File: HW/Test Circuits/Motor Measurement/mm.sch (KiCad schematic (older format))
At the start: 20 parts, among them J1 IN, J2 MOTOR, J3 PWR, J4 OUT, U1 MCP6002

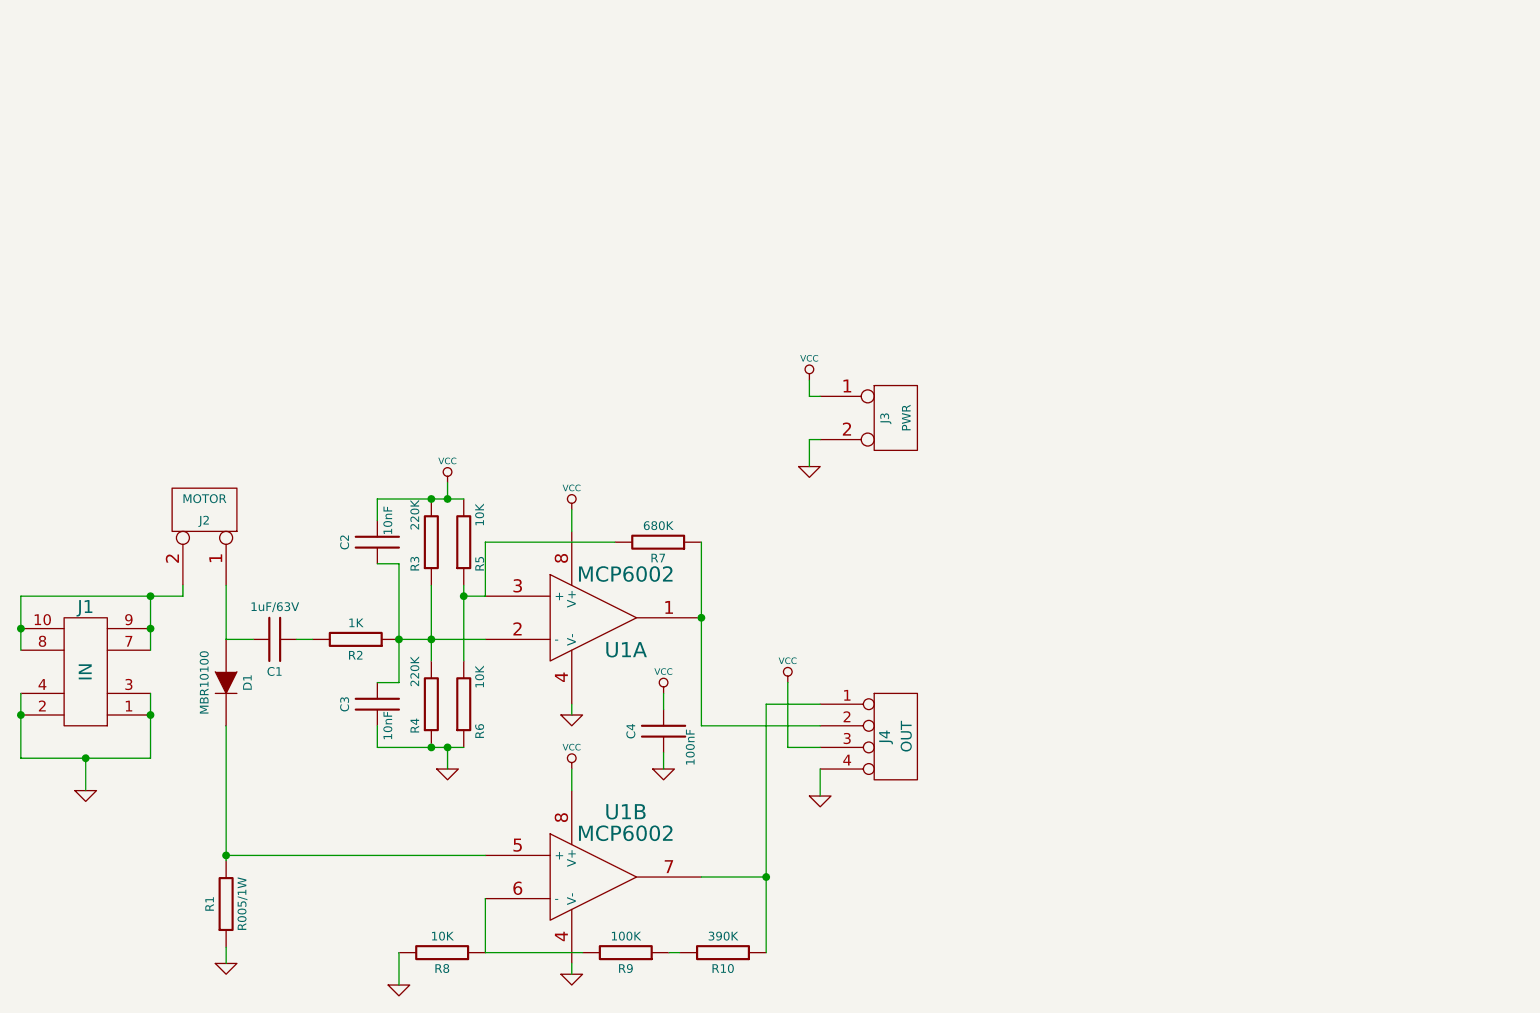
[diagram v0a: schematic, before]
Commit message: Driver schematic (unfinished)
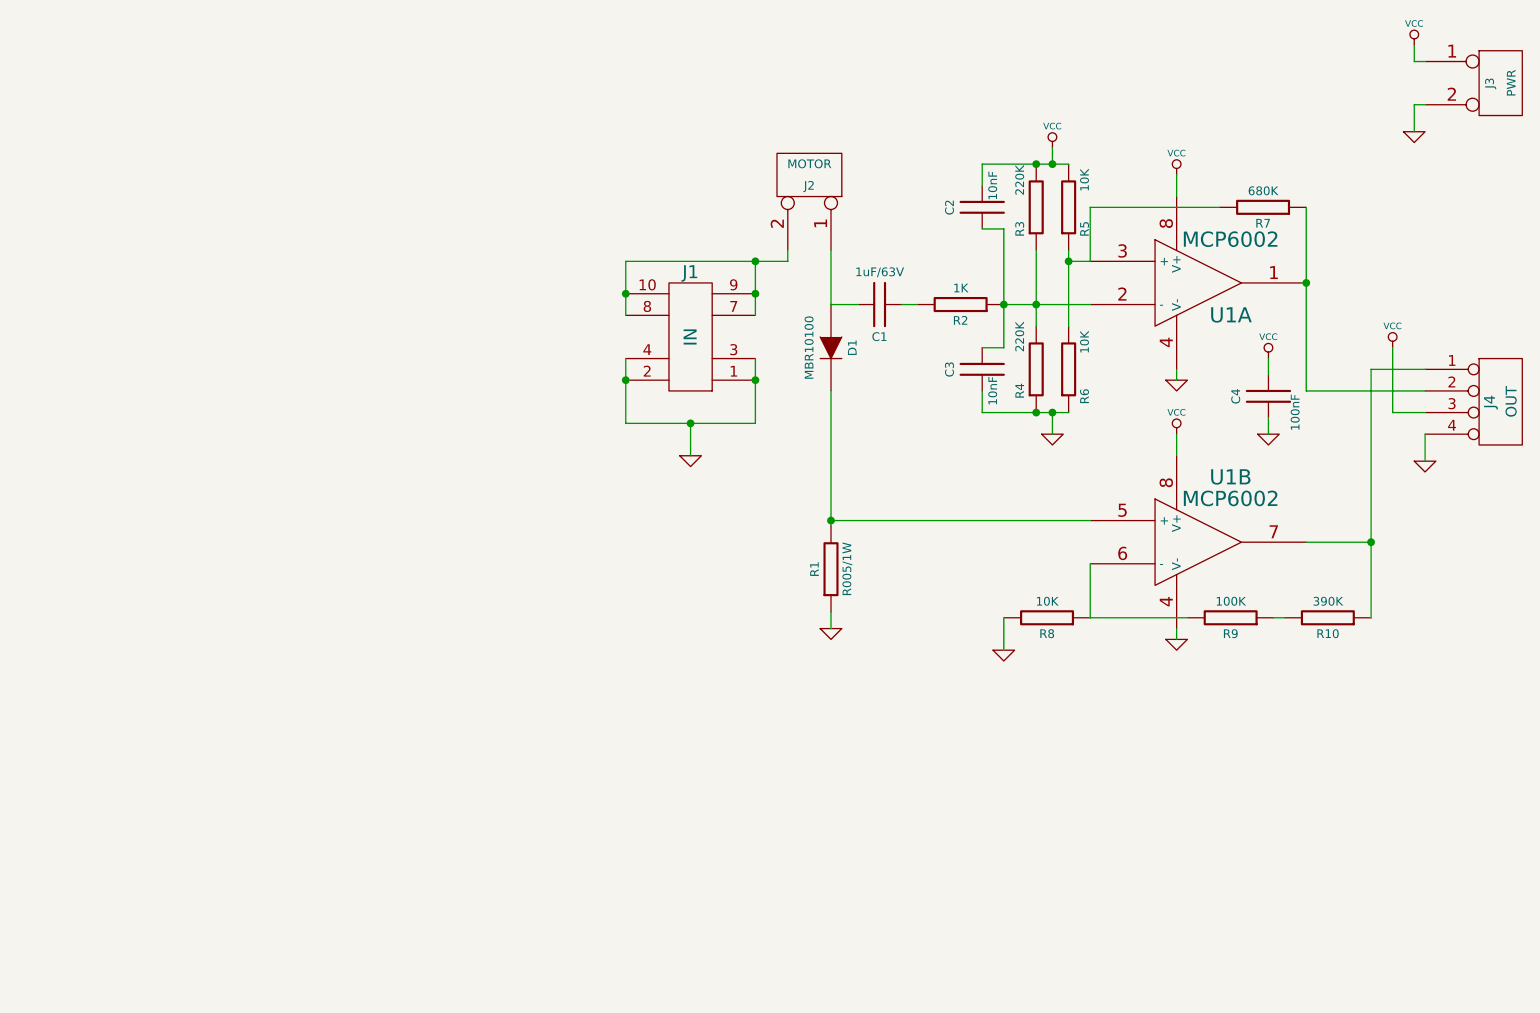
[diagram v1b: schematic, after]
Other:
- moved on the sheet: C1, C2, C3, C4, D1, J1, J2, J3, J4, R1, R10, R2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
